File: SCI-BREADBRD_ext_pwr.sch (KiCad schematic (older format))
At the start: 7 parts, among them P3 CONN_3, Q1 SI4564DY-T1-GE3

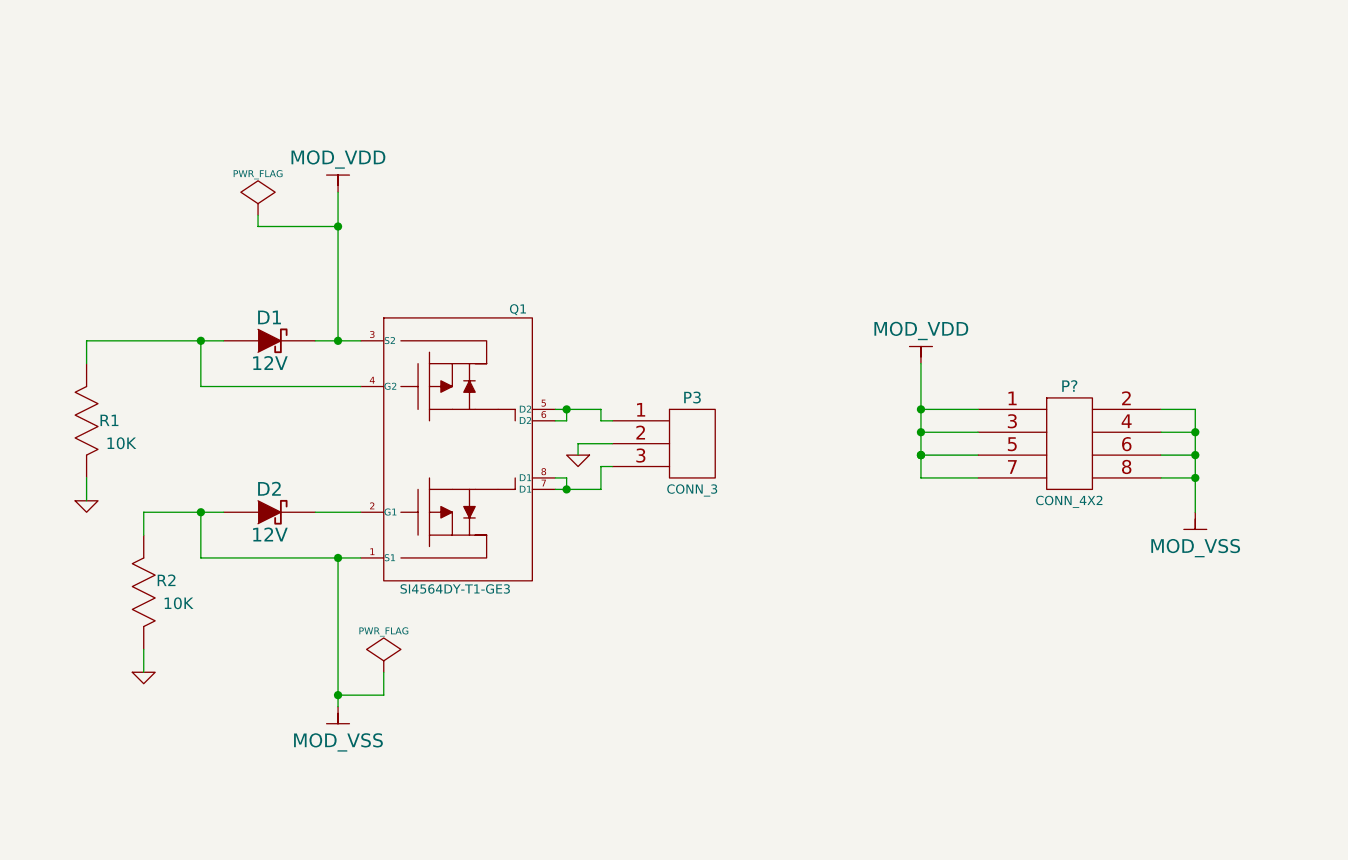
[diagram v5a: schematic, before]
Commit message: Re-annotated for added parts.
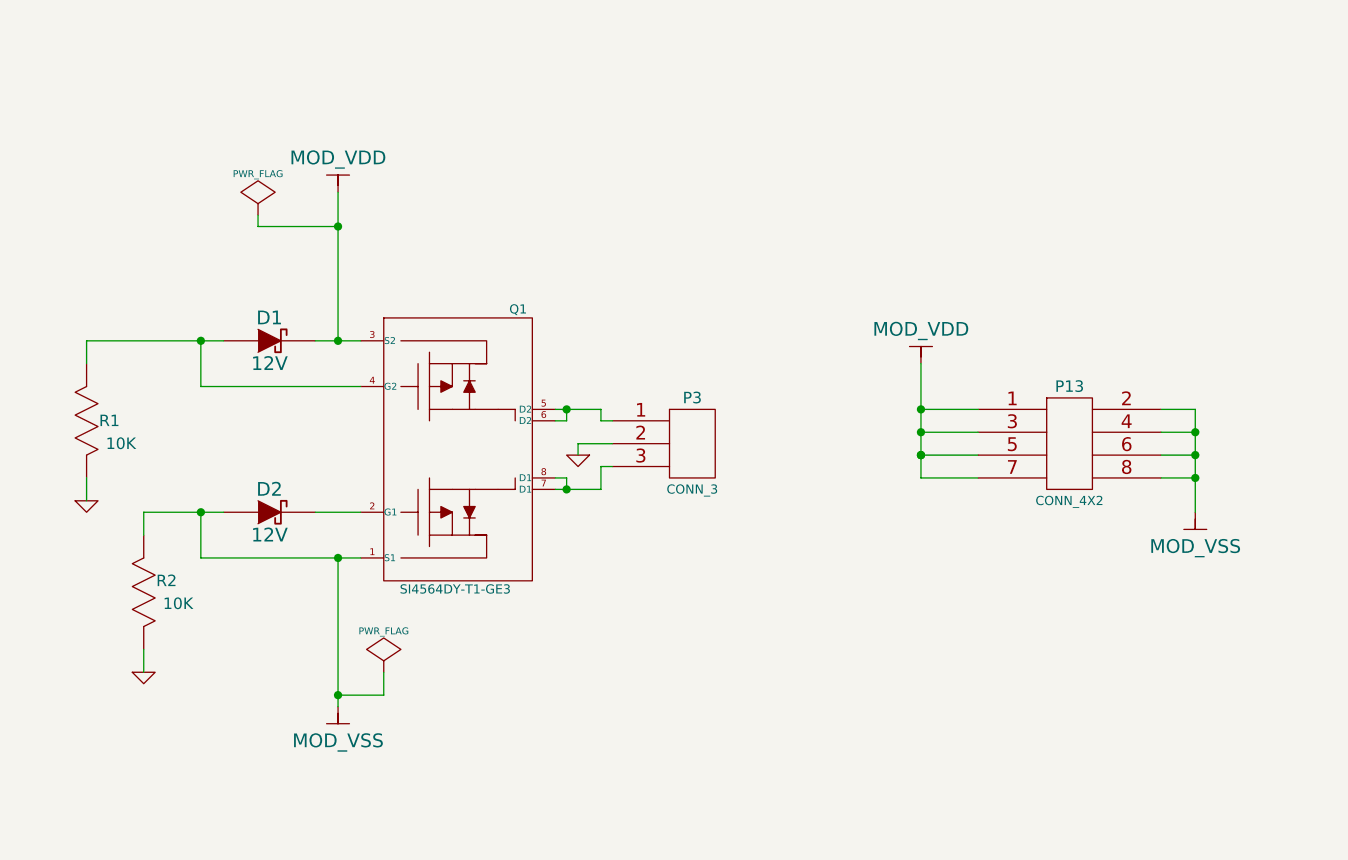
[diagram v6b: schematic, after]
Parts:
- gave numbers to parts that had none: 1
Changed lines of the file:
@@
-EESchema Schematic File Version 2  date Tue 01 May 2012 07:41:38 PM EDT
+EESchema Schematic File Version 2  date Wed 02 May 2012 02:37:03 AM EDT
 LIBS:custom_transistors
 LIBS:TI_custom
@@
 Sheet 4 9
 Title "SCI-BREADBRD-MVK"
-Date "1 may 2012"
+Date "2 may 2012"
 Rev "A"
 Comp "The Ohio State University"
@@
 $EndComp
 $Comp
-L GND #PWR13
+L GND #PWR07
 U 1 1 4F9A6338
 P 5250 3900
-F 0 "#PWR13" H 5250 3900 30  0001 C CNN
+F 0 "#PWR07" H 5250 3900 30  0001 C CNN
 F 1 "GND" H 5250 3830 30  0001 C CNN
 	1    5250 3900
@@
 $EndComp
 $Comp
-L GND #PWR7
+L GND #PWR08
 U 1 1 4F9A6362
 P 3100 4100
-F 0 "#PWR7" H 3100 4100 30  0001 C CNN
+F 0 "#PWR08" H 3100 4100 30  0001 C CNN
 F 1 "GND" H 3100 4030 30  0001 C CNN
 	1    3100 4100
@@
 $EndComp
 $Comp
-L GND #PWR8
+L GND #PWR09
 U 1 1 4F9A6368
 P 3350 4850
-F 0 "#PWR8" H 3350 4850 30  0001 C CNN
+F 0 "#PWR09" H 3350 4850 30  0001 C CNN
 F 1 "GND" H 3350 4780 30  0001 C CNN
 	1    3350 4850
@@
 $EndComp
 $Comp
-L PWR_FLAG #FLG2
+L PWR_FLAG #FLG010
 U 1 1 4F9AE522
 P 3850 2850
-F 0 "#FLG2" H 3850 2945 30  0001 C CNN
+F 0 "#FLG010" H 3850 2945 30  0001 C CNN
 F 1 "PWR_FLAG" H 3850 3030 30  0000 C CNN
 	1    3850 2850
@@
 $EndComp
 $Comp
-L PWR_FLAG #FLG1
+L PWR_FLAG #FLG011
 U 1 1 4F9AE5B3
 P 4400 4850
-F 0 "#FLG1" H 4400 4945 30  0001 C CNN
+F 0 "#FLG011" H 4400 4945 30  0001 C CNN
 F 1 "PWR_FLAG" H 4400 5030 30  0000 C CNN
 	1    4400 4850
@@
 $EndComp
 $Comp
-L MOD_VDD #PWR?
+L MOD_VDD #PWR012
 U 1 1 4F9AEB3C
 P 4200 2750
-F 0 "#PWR?" H 4200 2850 30  0001 C CNN
+F 0 "#PWR012" H 4200 2850 30  0001 C CNN
 F 1 "MOD_VDD" H 4200 2900 60  0000 C CNN
 	1    4200 2750
@@
 $EndComp
 $Comp
-L MOD_VSS #PWR?
+L MOD_VSS #PWR013
 U 1 1 4F9AEBAB
 P 4200 5000
-F 0 "#PWR?" H 4200 4900 30  0001 C CNN
+F 0 "#PWR013" H 4200 4900 30  0001 C CNN
 F 1 "MOD_VSS" H 4200 4850 60  0000 C CNN
 	1    4200 5000
@@
 $EndComp
 $Comp
-L MOD_VDD #PWR?
+L MOD_VDD #PWR014
 U 1 1 4FA07404
 P 6750 3500
-F 0 "#PWR?" H 6750 3600 30  0001 C CNN
+F 0 "#PWR014" H 6750 3600 30  0001 C CNN
 F 1 "MOD_VDD" H 6750 3650 60  0000 C CNN
 	1    6750 3500
@@
 $EndComp
 $Comp
-L MOD_VSS #PWR?
+L MOD_VSS #PWR015
 U 1 1 4FA07672
 P 7950 4150
-F 0 "#PWR?" H 7950 4050 30  0001 C CNN
+F 0 "#PWR015" H 7950 4050 30  0001 C CNN
 F 1 "MOD_VSS" H 7950 4000 60  0000 C CNN
 	1    7950 4150
@@
 $EndComp
 $Comp
-L CONN_4X2 P?
+L CONN_4X2 P13
 U 1 1 4FA07891
 P 7400 3850
-F 0 "P?" H 7400 4100 50  0000 C CNN
+F 0 "P13" H 7400 4100 50  0000 C CNN
 F 1 "CONN_4X2" H 7400 3600 40  0000 C CNN
 F 2 "pin_array_4x2" H 7400 3850 60  0001 C CNN
@@
 $EndComp
 Wire Wire Line
-	5150 3700 5200 3700
-Wire Wire Line
-	5200 3700 5350 3700
+	5150 3700 5350 3700
 Wire Wire Line
 	5200 3700 5200 3750
@@
 	5200 4000 5200 4050
 Wire Wire Line
-	5150 4050 5200 4050
-Wire Wire Line
-	5200 4050 5350 4050
+	5150 4050 5350 4050
 Wire Wire Line
 	5350 4050 5350 3950
@@
 Connection ~ 4200 3400
 Wire Wire Line
-	3100 3400 3600 3400
-Wire Wire Line
-	3600 3400 3700 3400
+	3100 3400 3700 3400
 Wire Wire Line
 	3100 4100 3100 4000
@@
 	3350 4850 3350 4750
 Wire Wire Line
-	4200 4350 4200 4950
-Wire Wire Line
-	4200 4950 4200 5000
+	4200 4350 4200 5000
 Connection ~ 4200 4350
 Wire Wire Line
@@
 	3350 4250 3350 4150
 Wire Wire Line
-	3350 4150 3600 4150
-Wire Wire Line
-	3600 4150 3700 4150
+	3350 4150 3700 4150
 Wire Wire Line
 	3850 2900 4200 2900
 Wire Wire Line
-	4200 2750 4200 2900
-Wire Wire Line
-	4200 2900 4200 3400
-Wire Wire Line
-	4100 3400 4200 3400
-Wire Wire Line
-	4200 3400 4300 3400
-Wire Wire Line
-	3600 4350 4200 4350
-Wire Wire Line
-	4200 4350 4300 4350
+	4200 2750 4200 3400
+Wire Wire Line
+	4100 3400 4300 3400
+Wire Wire Line
+	3600 4350 4300 4350
 Wire Wire Line
 	3850 2850 3850 2900
@@
 	4400 4850 4400 4950
 Wire Wire Line
-	6750 3500 6750 3700
-Wire Wire Line
-	6750 3700 6750 3800
-Wire Wire Line
-	6750 3800 6750 3900
-Wire Wire Line
-	6750 3900 6750 4000
+	6750 3500 6750 4000
 Wire Wire Line
 	6750 4000 7000 4000
@@
 Connection ~ 6750 3700
 Wire Wire Line
-	7950 3700 7950 3800
-Wire Wire Line
-	7950 3800 7950 3900
-Wire Wire Line
-	7950 3900 7950 4000
-Wire Wire Line
-	7950 4000 7950 4150
+	7950 3700 7950 4150
 Wire Wire Line
 	7950 3700 7800 3700

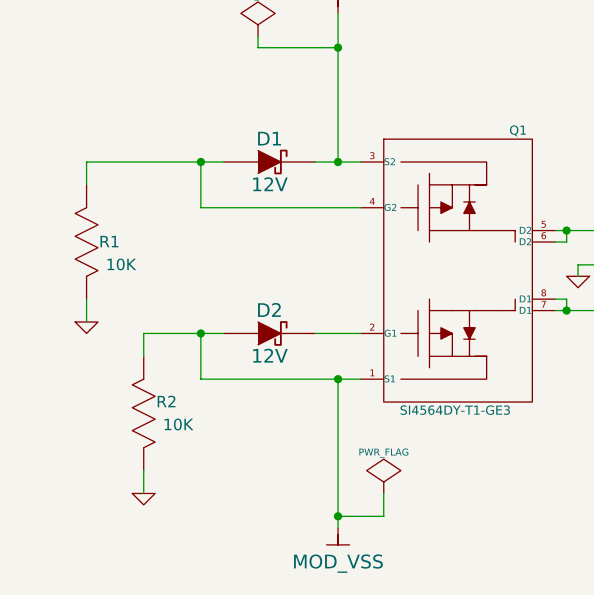
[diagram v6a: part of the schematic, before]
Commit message: Added some bypass caps. Rearranged pins on connectors to make layout easier.
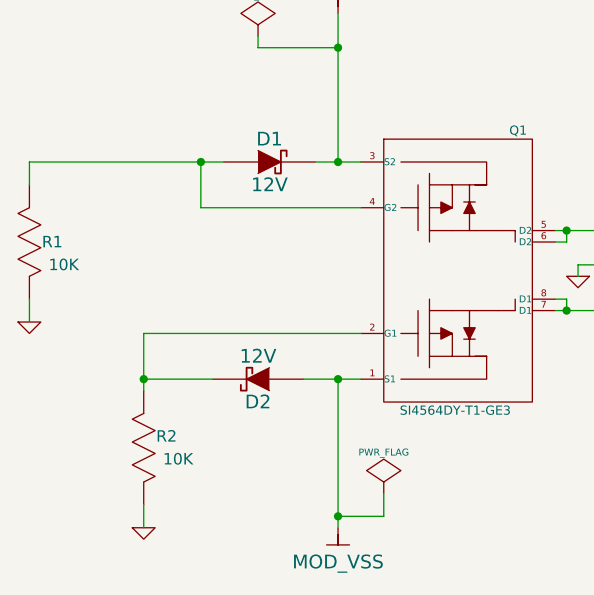
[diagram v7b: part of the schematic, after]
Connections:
- net MOD_VSS: no longer R2.2 (B)
- net at D2.2 (K), Q1.2 (G1): now also R2.2 (B)
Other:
- moved on the sheet: D2, R1, R2
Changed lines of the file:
@@
-EESchema Schematic File Version 2  date Wed 02 May 2012 02:37:03 AM EDT
+EESchema Schematic File Version 2  date Wed 02 May 2012 11:11:08 PM EDT
 LIBS:custom_transistors
 LIBS:TI_custom
@@
 Sheet 4 9
 Title "SCI-BREADBRD-MVK"
-Date "2 may 2012"
+Date "3 may 2012"
 Rev "A"
 Comp "The Ohio State University"
@@
 L R_US R2
 U 1 1 4F9A6341
-P 3350 4500
-F 0 "R2" V 3400 4400 50  0000 C CNN
-F 1 "10K" V 3300 4350 50  0000 C CNN
-F 2 "0402" H 3350 4500 60  0001 C CNN
-F 4 "Panasonic - ECG" H 3350 4500 60  0001 C CNN "Manufacturer"
-F 5 "ERJ-2GEJ103X" H 3350 4500 60  0001 C CNN "Part Number"
-F 6 "RES Thick Film 10K OHM 1/10W 5% 0402" H 3350 4500 60  0001 C CNN "Description"
-	1    3350 4500
+P 3350 4650
+F 0 "R2" V 3400 4550 50  0000 C CNN
+F 1 "10K" V 3300 4500 50  0000 C CNN
+F 2 "0402" H 3350 4650 60  0001 C CNN
+F 4 "Panasonic - ECG" H 3350 4650 60  0001 C CNN "Manufacturer"
+F 5 "ERJ-2GEJ103X" H 3350 4650 60  0001 C CNN "Part Number"
+F 6 "RES Thick Film 10K OHM 1/10W 5% 0402" H 3350 4650 60  0001 C CNN "Description"
+	1    3350 4650
 	0    -1   -1   0
 $EndComp
@@
 L R_US R1
 U 1 1 4F9A634A
-P 3100 3750
-F 0 "R1" V 3100 3650 50  0000 C CNN
-F 1 "10K" V 3000 3600 50  0000 C CNN
-F 2 "0402" H 3100 3750 60  0001 C CNN
-F 4 "Panasonic - ECG" H 3100 3750 60  0001 C CNN "Manufacturer"
-F 5 "ERJ-2GEJ103X" H 3100 3750 60  0001 C CNN "Part Number"
-F 6 "RES Thick Film 10K OHM 1/10W 5% 0402" H 3100 3750 60  0001 C CNN "Description"
-	1    3100 3750
+P 2850 3750
+F 0 "R1" V 2850 3650 50  0000 C CNN
+F 1 "10K" V 2750 3600 50  0000 C CNN
+F 2 "0402" H 2850 3750 60  0001 C CNN
+F 4 "Panasonic - ECG" H 2850 3750 60  0001 C CNN "Manufacturer"
+F 5 "ERJ-2GEJ103X" H 2850 3750 60  0001 C CNN "Part Number"
+F 6 "RES Thick Film 10K OHM 1/10W 5% 0402" H 2850 3750 60  0001 C CNN "Description"
+	1    2850 3750
 	0    -1   -1   0
 $EndComp
@@
 L DIODESCH D2
 U 1 1 4F9A635C
-P 3900 4150
-F 0 "D2" H 3900 4250 60  0000 C CNN
-F 1 "12V" H 3900 4050 60  0000 C CNN
-F 2 "SOT_23_ON" H 3900 4150 60  0001 C CNN
-F 4 "ON Semiconductor" H 3900 4150 60  0001 C CNN "Manufacturer"
-F 5 "BZX84C12LT1G" H 3900 4150 60  0001 C CNN "Part Number"
-F 6 "DIODE ZENER 12V 225MW SOT-23" H 3900 4150 60  0001 C CNN "Description"
-	1    3900 4150
-	1    0    0    -1
+P 3850 4350
+F 0 "D2" H 3850 4450 60  0000 C CNN
+F 1 "12V" H 3850 4250 60  0000 C CNN
+F 2 "SOT_23_ON" H 3850 4350 60  0001 C CNN
+F 4 "ON Semiconductor" H 3850 4350 60  0001 C CNN "Manufacturer"
+F 5 "BZX84C12LT1G" H 3850 4350 60  0001 C CNN "Part Number"
+F 6 "DIODE ZENER 12V 225MW SOT-23" H 3850 4350 60  0001 C CNN "Description"
+	1    3850 4350
+	-1   0    0    1
 $EndComp
 $Comp
 L GND #PWR08
 U 1 1 4F9A6362
-P 3100 4100
-F 0 "#PWR08" H 3100 4100 30  0001 C CNN
-F 1 "GND" H 3100 4030 30  0001 C CNN
-	1    3100 4100
+P 2850 4100
+F 0 "#PWR08" H 2850 4100 30  0001 C CNN
+F 1 "GND" H 2850 4030 30  0001 C CNN
+	1    2850 4100
 	1    0    0    -1
 $EndComp
@@
 L GND #PWR09
 U 1 1 4F9A6368
-P 3350 4850
-F 0 "#PWR09" H 3350 4850 30  0001 C CNN
-F 1 "GND" H 3350 4780 30  0001 C CNN
-	1    3350 4850
+P 3350 5000
+F 0 "#PWR09" H 3350 5000 30  0001 C CNN
+F 1 "GND" H 3350 4930 30  0001 C CNN
+	1    3350 5000
 	1    0    0    -1
 $EndComp
@@
 Connection ~ 4200 3400
 Wire Wire Line
-	3100 3400 3700 3400
-Wire Wire Line
-	3100 4100 3100 4000
+	2850 3400 3700 3400
+Wire Wire Line
+	2850 4100 2850 4000
 Wire Wire Line
 	3600 3400 3600 3600
@@
 Connection ~ 3600 3400
 Wire Wire Line
-	4100 4150 4300 4150
-Wire Wire Line
-	3600 4350 3600 4150
-Connection ~ 3600 4150
-Wire Wire Line
-	3350 4850 3350 4750
+	3350 5000 3350 4900
 Wire Wire Line
 	4200 4350 4200 5000
 Connection ~ 4200 4350
 Wire Wire Line
-	3100 3500 3100 3400
-Wire Wire Line
-	3350 4250 3350 4150
-Wire Wire Line
-	3350 4150 3700 4150
+	2850 3500 2850 3400
 Wire Wire Line
 	3850 2900 4200 2900
@@
 	4100 3400 4300 3400
 Wire Wire Line
-	3600 4350 4300 4350
+	4050 4350 4300 4350
 Wire Wire Line
 	3850 2850 3850 2900
@@
 	4400 4950 4200 4950
 Connection ~ 4200 4950
+Wire Wire Line
+	3650 4350 3350 4350
+Connection ~ 3350 4350
+Wire Wire Line
+	3350 4150 3350 4400
+Wire Wire Line
+	3350 4150 4300 4150
 $EndSCHEMATC

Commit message: More layout progress
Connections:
- net labels added: HI_VDD, HI_VSS
- net labels removed: MOD_VDD, MOD_VSS
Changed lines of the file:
@@
-EESchema Schematic File Version 2  date Wed 02 May 2012 11:11:08 PM EDT
+EESchema Schematic File Version 2  date Fri 04 May 2012 05:19:19 PM EDT
 LIBS:custom_transistors
 LIBS:TI_custom
@@
 Sheet 4 9
 Title "SCI-BREADBRD-MVK"
-Date "3 may 2012"
+Date "4 may 2012"
 Rev "A"
 Comp "The Ohio State University"
@@
 $EndComp
 $Comp
-L MOD_VDD #PWR012
-U 1 1 4F9AEB3C
-P 4200 2750
-F 0 "#PWR012" H 4200 2850 30  0001 C CNN
-F 1 "MOD_VDD" H 4200 2900 60  0000 C CNN
-	1    4200 2750
-	1    0    0    -1
-$EndComp
-$Comp
-L MOD_VSS #PWR013
-U 1 1 4F9AEBAB
-P 4200 5000
-F 0 "#PWR013" H 4200 4900 30  0001 C CNN
-F 1 "MOD_VSS" H 4200 4850 60  0000 C CNN
-	1    4200 5000
-	1    0    0    -1
-$EndComp
-$Comp
-L MOD_VDD #PWR014
-U 1 1 4FA07404
-P 6750 3500
-F 0 "#PWR014" H 6750 3600 30  0001 C CNN
-F 1 "MOD_VDD" H 6750 3650 60  0000 C CNN
-	1    6750 3500
-	1    0    0    -1
-$EndComp
-$Comp
-L MOD_VSS #PWR015
-U 1 1 4FA07672
-P 7950 4150
-F 0 "#PWR015" H 7950 4050 30  0001 C CNN
-F 1 "MOD_VSS" H 7950 4000 60  0000 C CNN
-	1    7950 4150
-	1    0    0    -1
-$EndComp
-$Comp
 L CONN_4X2 P13
 U 1 1 4FA07891
@@
 Wire Wire Line
 	3350 4150 4300 4150
+$Comp
+L HI_VDD #PWR?
+U 1 1 4FA44E90
+P 4200 2750
+F 0 "#PWR?" H 4200 2850 30  0001 C CNN
+F 1 "HI_VDD" H 4200 2900 60  0000 C CNN
+	1    4200 2750
+	1    0    0    -1
+$EndComp
+$Comp
+L HI_VSS #PWR?
+U 1 1 4FA44E9F
+P 4200 5000
+F 0 "#PWR?" H 4200 4900 30  0001 C CNN
+F 1 "HI_VSS" H 4200 4850 60  0000 C CNN
+	1    4200 5000
+	1    0    0    -1
+$EndComp
+$Comp
+L HI_VDD #PWR?
+U 1 1 4FA44EAC
+P 6750 3500
+F 0 "#PWR?" H 6750 3600 30  0001 C CNN
+F 1 "HI_VDD" H 6750 3650 60  0000 C CNN
+	1    6750 3500
+	1    0    0    -1
+$EndComp
+$Comp
+L HI_VSS #PWR?
+U 1 1 4FA44EBC
+P 7950 4150
+F 0 "#PWR?" H 7950 4050 30  0001 C CNN
+F 1 "HI_VSS" H 7950 4000 60  0000 C CNN
+	1    7950 4150
+	1    0    0    -1
+$EndComp
 $EndSCHEMATC
